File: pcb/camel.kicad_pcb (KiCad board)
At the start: 4 copper layers, 57 x 28 mm, 56 parts, among them J1 Conn_01x04, J2 Conn_01x04, J3 TC2030-NL, J4 USART, J5 Conn_01x04, J6 I2C STEMMA, U1 MCP1700T-3302E/TT, U2 HX712, U3 STM32L010F4P6, U4 HX712

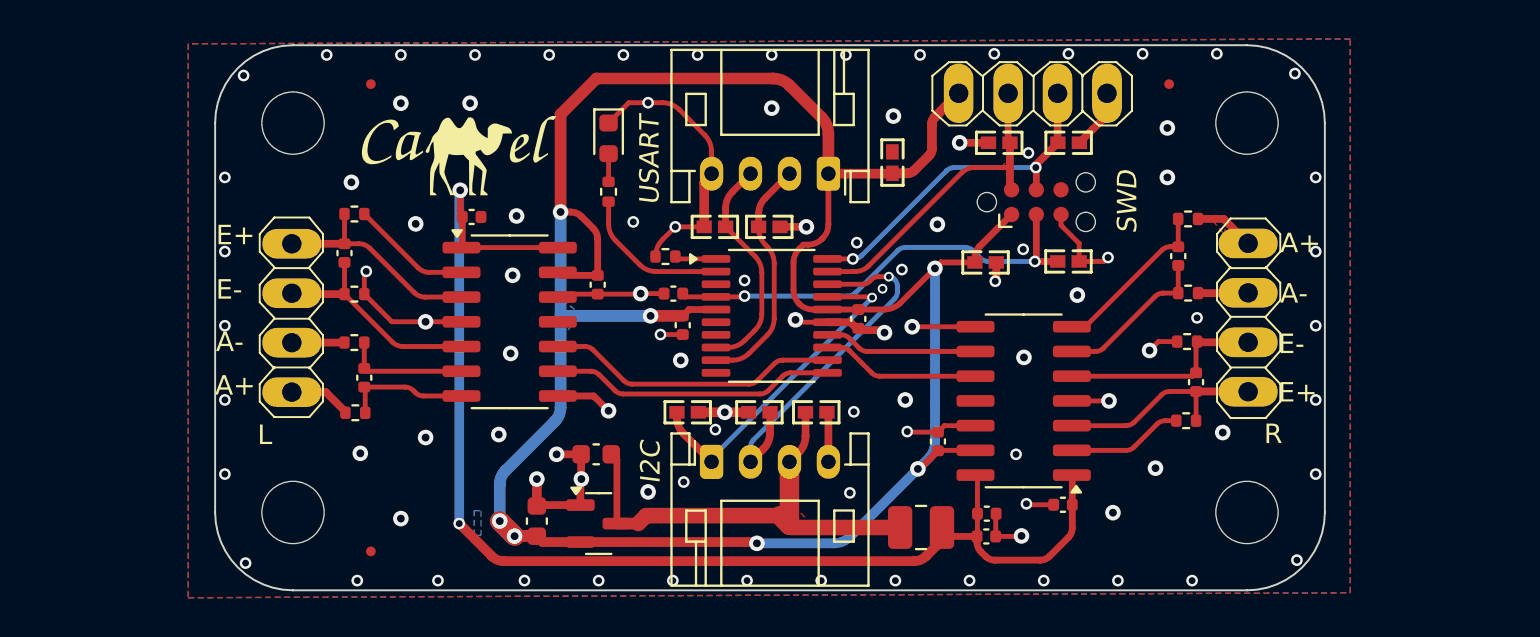
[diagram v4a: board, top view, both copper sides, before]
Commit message: PCB refactoring, BOM updates, firmware added EEPROM storage of configuration
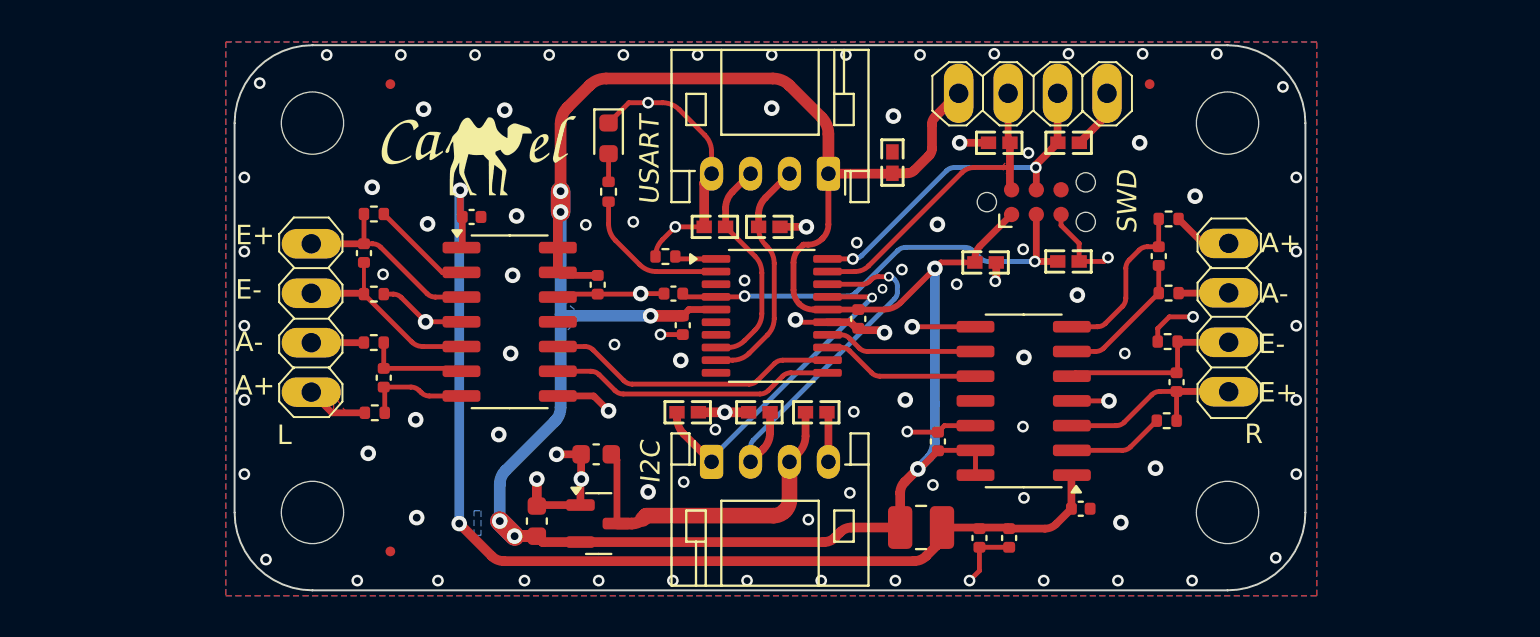
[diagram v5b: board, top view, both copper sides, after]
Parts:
- moved C3 1.69 mm to (160.8, 116.3), turned to -90 degrees
- moved G*** 1.02 mm to (133.6, 96.7)
- moved C12 1.00 mm to (128.7, 108.1)
- moved R1 1.00 mm to (128.2, 99.7)
- moved C11 1.00 mm to (127.6, 101.7)
- moved C14 1.00 mm to (169.4, 108.3)
- moved C15 1.00 mm to (168.5, 101.8)
- moved FID1 1.00 mm to (168.0, 93.0)
- moved FID2 1.00 mm to (129.0, 93.0)
- moved FID3 1.00 mm to (129.0, 117.0)
- moved H1 1.00 mm to (125.0, 95.0)
- moved H2 1.00 mm to (172.0, 115.0)
- moved H3 1.00 mm to (172.0, 95.0)
- moved H4 1.00 mm to (125.0, 115.0)
- moved J1 1.00 mm to (124.9, 101.2)
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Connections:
- L1 pad 2: VDD -> +3V3
- U2 pad 14: VDDA -> +3V3
- U4 pad 14: VDDA -> +3V3
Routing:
- net VDDA: track 65.9 -> 55.5 mm
- net VDD: track 24.6 -> 17.9 mm
- net +3V3: track 124.7 -> 126.7 mm
- net GND: track 74.6 -> 73.0 mm, vias 99 -> 102
- net /L_REFN: track 11.4 -> 10.4 mm
- net /L_INP: track 6.47 -> 5.47 mm
- net /L_INN: track 6.38 -> 5.38 mm
- net /R_REFN: track 10.7 -> 9.72 mm
- net /R_REFP: track 11.2 -> 10.2 mm
- net /L_REFP: track 11.3 -> 10.3 mm
- net /R_VOUT: track 5.93 -> 4.96 mm
- net /R_INN: track 8.07 -> 7.10 mm
- net /L_VOUT: track 6.19 -> 5.23 mm
- added copper zone on F.Cu, net Net-(J1-Pin_4)
- removed copper zone on F.Cu, net Net-(J5-Pin_4)
- removed copper zone on F.Cu, net VDD
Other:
- board size 57 x 28 mm -> 55 x 28 mm

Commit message: PCBway additions
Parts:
- C1, C11, C12, C14, C15, C2: value 0.1u -> 100n
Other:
- board text added: "WayWayWay"
- board text removed: "JLCJLCJLCJLC"

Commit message: updated STM32CubeMX version, updating to STM32L031F6
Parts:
- U3: value STM32L010F4P6 -> STM32L031F6P6
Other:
- board text added: "${FAB_ON_PLACEHOLDER}"
- board text removed: "WayWayWay"

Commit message: version 3.0 update MCU and VDD on USART connector, prepare for JLCPCB
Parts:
- added D12: RCLAMP0521P-N, camel:X1-DFN1006-2_L1.0-W0.6-BI, F.Cu at (142.3, 97.0)
- added REF01: QR, camel:camel_qrcode_5x5, B.Cu at (138.5, 94.8)
- moved D1 3.09 mm to (155.5, 94.0), turned to -90 degrees
- turned D7 to 180 degrees
- turned D8 to 0 degrees
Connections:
- D7 pad 1: /USART_RX -> GND
- D7 pad 2: GND -> /USART_RX
- D8 pad 1: /USART_TX -> GND
- D8 pad 2: GND -> /USART_TX
- J4 pad 1: +3V3 -> GND
- J4 pad 4: GND -> VDD
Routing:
- net VDD: track 17.9 -> 38.5 mm, vias 0 -> 2
- net +3V3: track 126.7 -> 110.7 mm
- net GND: track 73.0 -> 61.8 mm, vias 102 -> 108
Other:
- board text added: "Rev ${CAMEL_VERSION}"
- board text removed: "${FAB_ON_PLACEHOLDER}"
- board text removed: "Rev 2.0"
